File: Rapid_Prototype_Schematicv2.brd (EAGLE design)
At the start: 142 x 95 mm, 177 parts, among them IC1 OP-AMP, IC2 SI4459ADY-T1-GE3, IC3 OP-AMP, IC4 OP-AMP, IC5 OP-AMP, IC8 SI4485DY-T1-GE3, J1 XT60-M, J10 XT60-M, J2 XT60-M, J3 Vertical Qwiic Connector, J4 UJ2-MIBH-2-SMT-TR-67, J5 XT60-M, J6 XT60-M, J7 XT60-M, J8 XT60-M, J9 XT60-M, Q1 LTV-8141S, Q10 SI4435DDY, Q12 SI4435DDY, Q14 SI4435DDY, Q16 2N7002PW, Q2 2N7002PW, Q4 SI4435DDY, Q6 SI4435DDY, Q8 SI4435DDY, T1 2N3904, T2 2N3904, T3 2N3904, T4 2N3904, T5 2N3904, T6 2N3904, T7 2N3904, U1 LM35DM, U7 TLV1117LV33DCYR, U8 LT1374IS8-5PBF

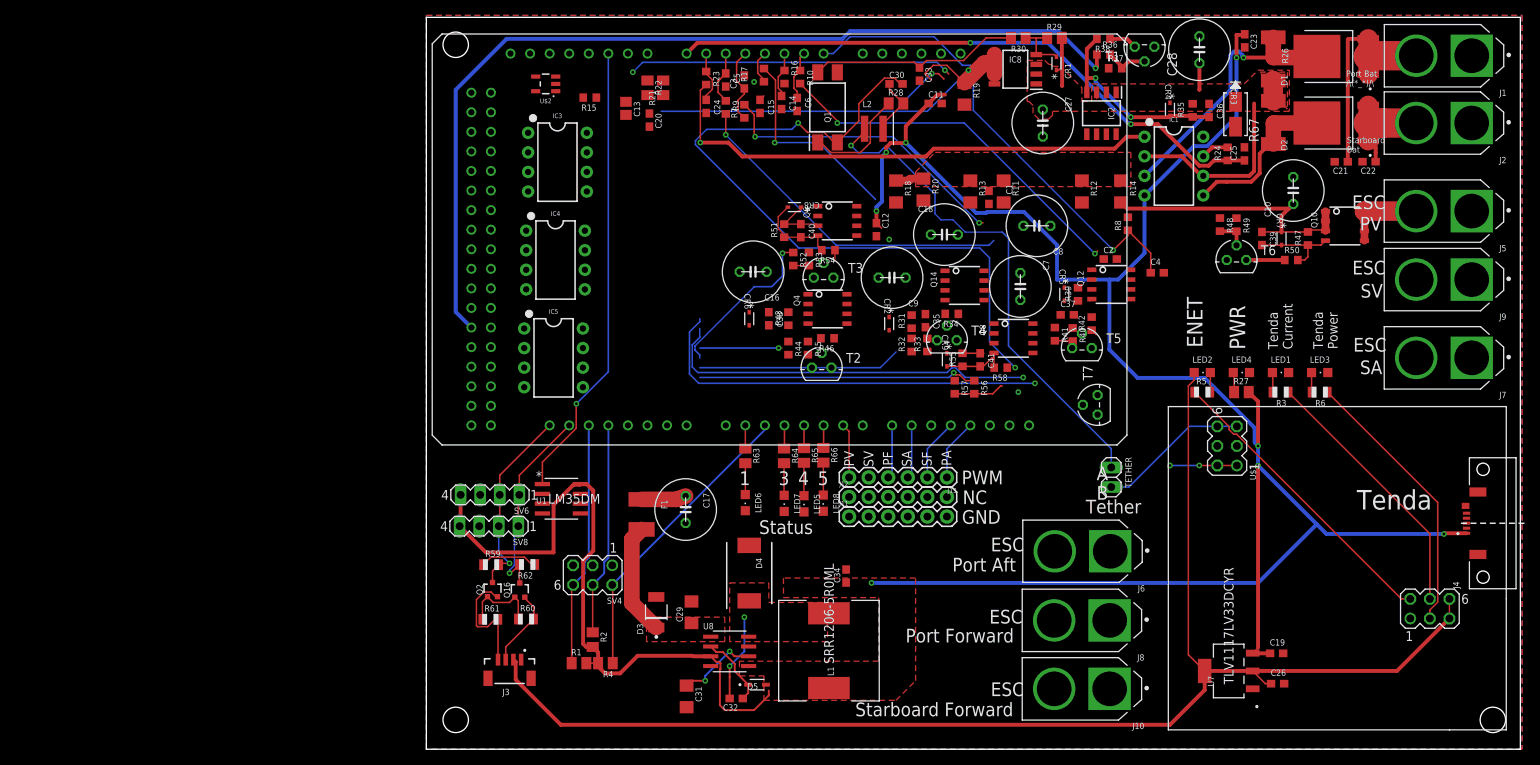
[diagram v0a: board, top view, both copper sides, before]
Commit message: Sebastian the man of progress
Re-employed the mainswitches and will route next meeting
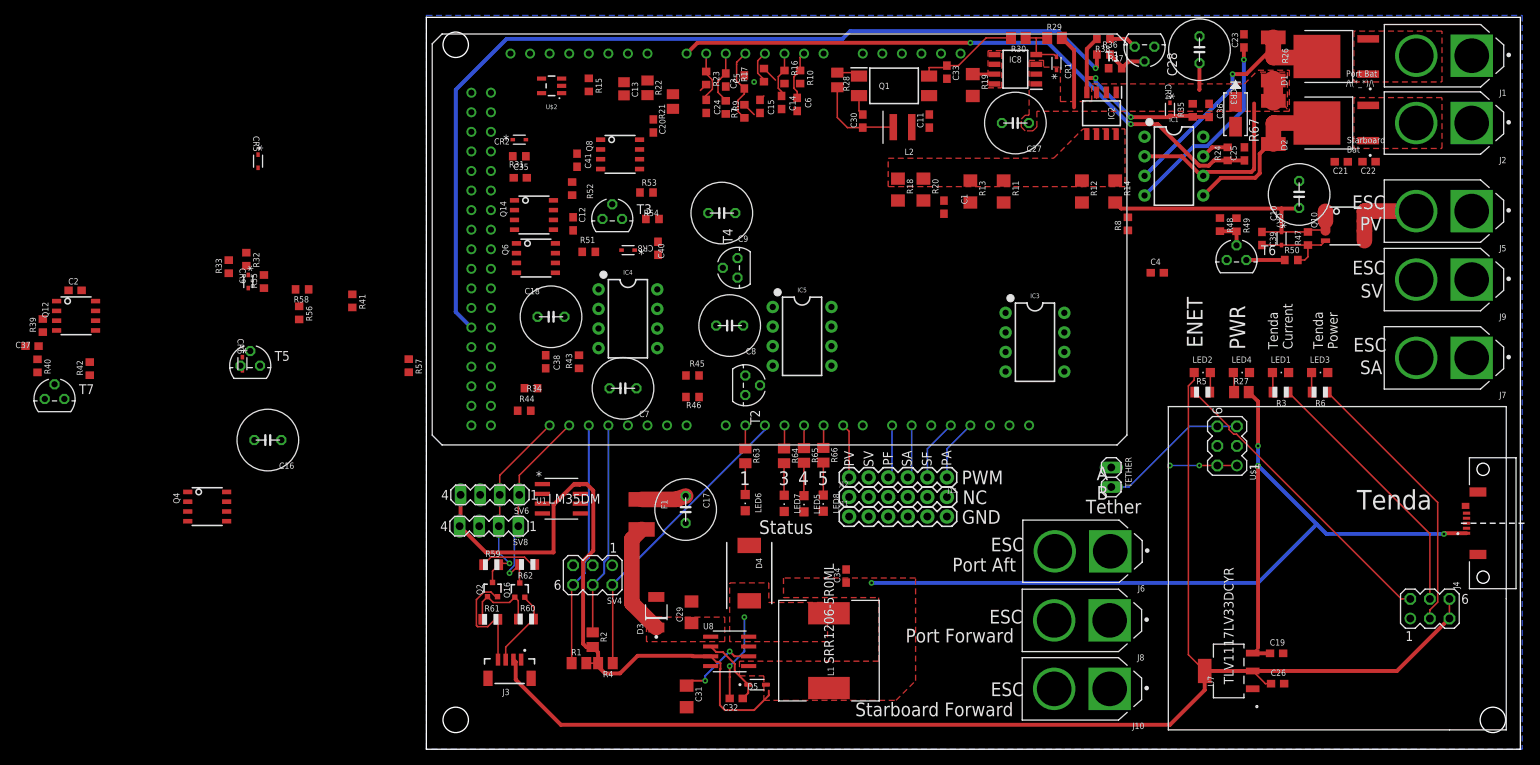
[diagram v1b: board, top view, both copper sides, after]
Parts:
- moved T7 135.4 mm to (-48.3, 45.5), turned to 0 degrees
- moved Q12 134.4 mm to (-45.5, 56.3)
- moved C2 134.4 mm to (-45.6, 59.6)
- moved C37 134.4 mm to (-51.2, 52.3)
- moved R39 134.4 mm to (-49.8, 55.0)
- moved R40 134.4 mm to (-50.5, 49.8)
- moved R42 130.2 mm to (-43.7, 49.4)
- moved T5 108.0 mm to (-22.9, 49.8)
- moved CR5 106.1 mm to (-21.8, 76.3)
- moved R41 91.3 mm to (-9.61, 58.2)
- moved R58 91.2 mm to (-16.1, 59.7)
- moved CR9 91.2 mm to (-23.1, 60.7)
- moved R33 91.2 mm to (-25.6, 62.6)
- moved R55 91.2 mm to (-21.1, 60.7)
- moved R56 88.2 mm to (-16.5, 56.6)
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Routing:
- net 5V: track 352.5 -> 242.1 mm, vias 8 -> 5
- net TETHER_B: track 113.9 -> 22.2 mm, vias 2 -> 0
- net N$34: track 67.3 -> 1.08 mm, vias 1 -> 0
- net TETHER_A: track 74.7 -> 9.05 mm, vias 3 -> 2
- net ESCPV_CURR: track 63.3 -> 0.00 mm, vias 1 -> 0
- net BTMP: track 59.4 -> 0.30 mm, vias 1 -> 0
- net CTLD_ELEC_PWR: track 60.1 -> 2.82 mm, vias 1 -> 0
- net ESCPV_SWITCH: track 53.4 -> 0.00 mm, vias 1 -> 0
- net ESCSV_SWITCH: track 49.4 -> 0.00 mm, vias 1 -> 0
- net O2: track 48.1 -> 0.00 mm, vias 2 -> 0
- net N$11: track 43.7 -> 0.00 mm, vias 1 -> 0
- net N$36: track 42.2 -> 0.00 mm, vias 2 -> 0
- net N$9: track 39.0 -> 1.81 mm, vias 2 -> 0
- net ESCSA_SWITCH: track 36.3 -> 0.00 mm, vias 1 -> 0
- net P_BATT+: track 29.4 -> 0.00 mm
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- added copper zone on layer 1, net CTLD_ELEC_PWR
- added copper zone on layer 1, net P_BATT+
- added copper zone on layer 1, net S_BATT+
- removed copper zone on layer 1, net GND
